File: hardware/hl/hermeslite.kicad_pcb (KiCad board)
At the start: 4 copper layers, 100 x 100 mm, 498 parts, among them CN1 USBBlaster2, CN10 RFD2b, CN11 RFD2b, CN12 RFD2b, CN2 PS, CN3 MagJack, CN4 IO8, CN5 IO8, CN6 IO8, CN7 IO8, CN8 RFD2b, CN9 RFD2b, J1 JNC, J10 JNC, J11 JNC, J12 JNO, J13 JNO, J14 JNC, J15 JNC, J16 JNO, J17 JNO, J18 JNC, J19 JNC, J2 JNC, J20 JNC, J21 JNC, J22 JNC, J23 JNO, J24 JNC, J25 JNC, J26 JNC, J27 JNC, J3 JNO, J4 JNO, J5 JNO, J6 DNI, J7 JNO, J8 JNO, J9 JNC, K2 NA3WK-K, Q1 DMP3099L, Q2 NUD3124, Q3 LDMOS, Q4 LDMOS, Q5 2N7002K, T1 1:1 Z, T2 8:1 Z, T3 TRANSF4CTS, U1 EEPROM, U10 PE4259, U11 PE4259, U12 AP2204, U13 MAX11613, U14 LP2985, U15 MCP4661, U16 ST1S10, U17 TPS730, U18 LMV324, U2 FPGA, U3 ST1S10, U4 KSZ9031RN, U5 MCP4716, U6 5P49V5923, U7 AD9866BCPZ, U8 ST1S10, U9 OPA2677, X1 25MHz, X2 38.4MHz, X3 38.4MHz

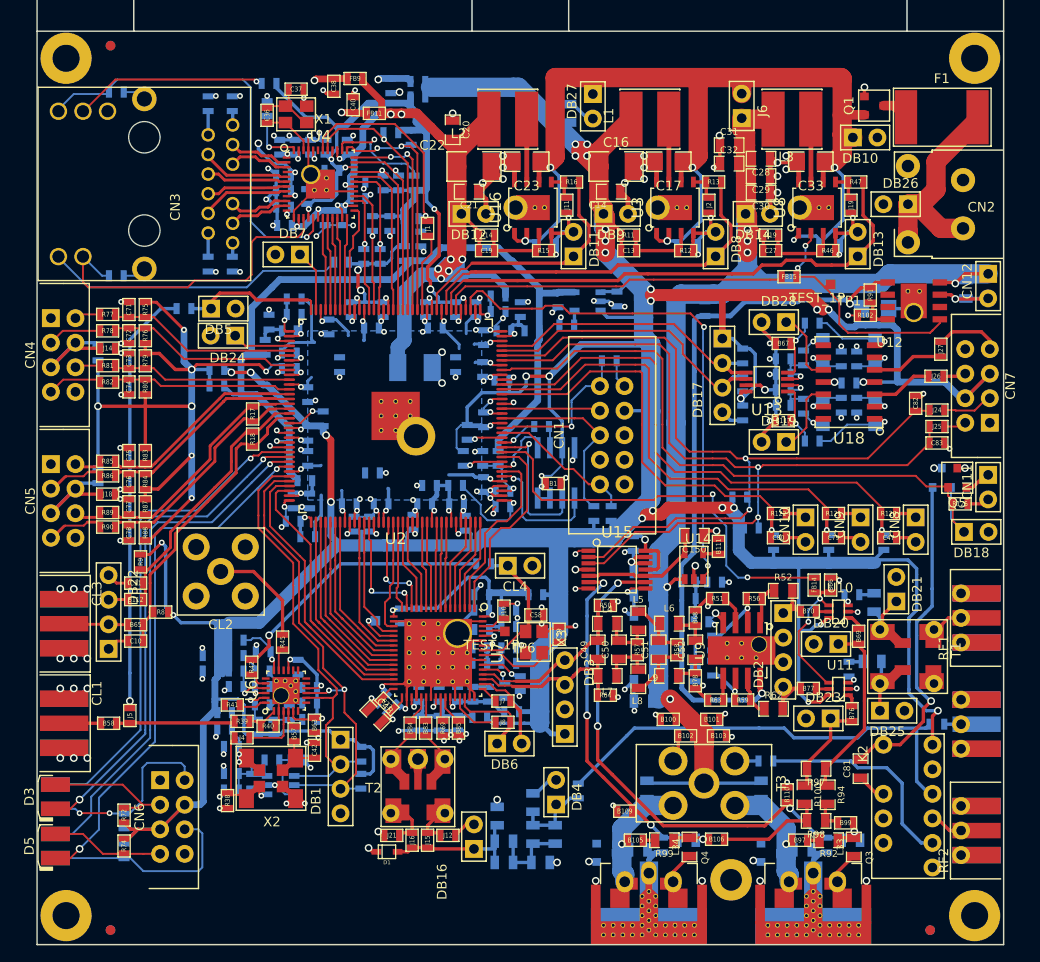
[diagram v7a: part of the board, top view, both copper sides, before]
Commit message: Layout silkscreen
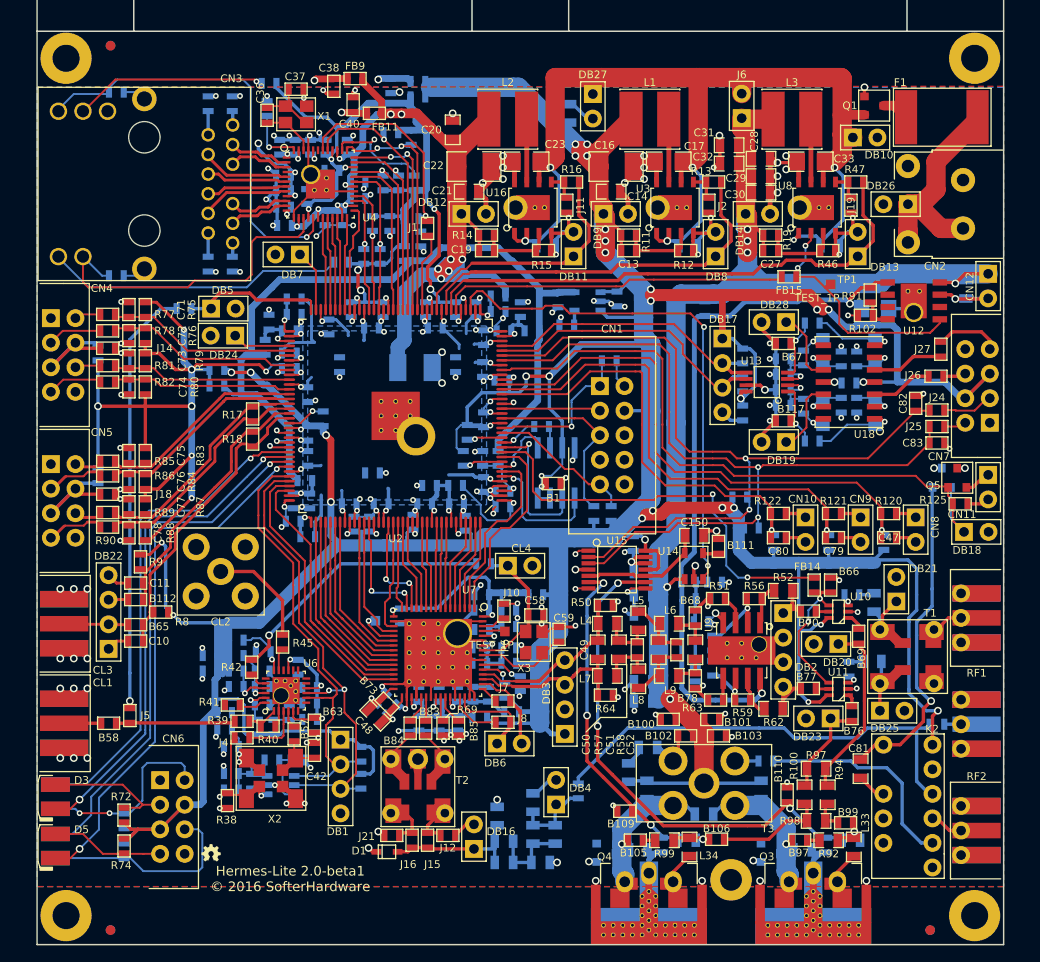
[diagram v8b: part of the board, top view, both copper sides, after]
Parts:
- added C84: 270pF, HERMESLITE:SMD-0805, B.Cu at (139.0, 126.5)
- added C85: DNI, HERMESLITE:SMD-0805, B.Cu at (131.2, 122.2)
- added G***: OSHW-logo_silkscreen-front_2mm, HERMESLITE:OSHW-logo_silkscreen-front_2mm, F.Cu at (88.0, 130.5)
- added G***: OSHW-logo_silkscreen-back_2mm, HERMESLITE:OSHW-logo_silkscreen-back_2mm, B.Cu at (105.5, 132.6)
- added R60: DNI, HERMESLITE:SMD-0805, B.Cu at (133.2, 119.6)
- L33, L34: value 100nH -> 0nH
- R100, R94: value 10 -> 14
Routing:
- net Net-(B97-Pad1): track 20.4 -> 23.1 mm
- net Net-(B105-Pad1): track 18.2 -> 20.9 mm
- net GND: track 567.8 -> 570.1 mm
- net Net-(C85-Pad1): track 0.00 -> 2.08 mm
- net +VPA: track 157.1 -> 159.1 mm
- added copper zone on B.Cu, net GND
- added copper zone on F.Cu, net GND
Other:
- board text added: "4 IO"
- board text added: "Hermes-Lite 2.0-beta1 © 2016 SofterHardware"
- board text added: "I2C 2 ANALOG"
- board text removed: "4 IO or Jumpers"
- board text removed: "Extra IO Slow Analog Inputs"
